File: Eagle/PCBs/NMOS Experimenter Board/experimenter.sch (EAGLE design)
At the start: 45 parts, among them U1 74HC14PW

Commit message: Wow, 92 transistors and 8 LEDs
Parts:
- added D2, D3, D4, D5, D6, D7, D8, D9: (no value), ellajameson-core:LED0603
- added DRAINA100, DRAINA101, DRAINA102, DRAINA103, DRAINA104, DRAINA105, DRAINA106, DRAINA107, DRAINA108, DRAINA109, DRAINA110, DRAINA111, DRAINA112, DRAINA2, DRAINA21, DRAINA22, DRAINA23, DRAINA24, DRAINA25, DRAINA26, DRAINA27, DRAINA28, DRAINA29, DRAINA3, DRAINA30, DRAINA31, DRAINA32, DRAINA33, DRAINA34, DRAINA35, DRAINA36, DRAINA37, DRAINA38, DRAINA39, DRAINA4, DRAINA40, DRAINA41, DRAINA42, DRAINA43, DRAINA44, DRAINA45, DRAINA46, DRAINA47, DRAINA48, DRAINA49, DRAINA5, DRAINA50, DRAINA51, DRAINA52, DRAINA53, DRAINA54, DRAINA55, DRAINA56, DRAINA57, DRAINA58, DRAINA59, DRAINA60, DRAINA61, DRAINA62, DRAINA63, DRAINA64, DRAINA65, DRAINA66, DRAINA67, DRAINA68, DRAINA69, DRAINA70, DRAINA71, DRAINA72, DRAINA73, DRAINA74, DRAINA75, DRAINA76, DRAINA77, DRAINA78, DRAINA79, DRAINA80, DRAINA81, DRAINA82, DRAINA83, DRAINA84, DRAINA85, DRAINA86, DRAINA87, DRAINA88, DRAINA89, DRAINA90, DRAINA91, DRAINA92, DRAINA93, DRAINA94, DRAINA95, DRAINA96, DRAINA97, DRAINA98, DRAINA99, DRAINB100, DRAINB101, DRAINB102, DRAINB103, DRAINB104, DRAINB105, DRAINB106, DRAINB107, DRAINB108, DRAINB109, DRAINB110, DRAINB111, DRAINB112, DRAINB2, DRAINB21, DRAINB22, DRAINB23, DRAINB24, DRAINB25, DRAINB26, DRAINB27, DRAINB28, DRAINB29, DRAINB3, DRAINB30, DRAINB31, DRAINB32, DRAINB33, DRAINB34, DRAINB35, DRAINB36, DRAINB37, DRAINB38, DRAINB39, DRAINB4, DRAINB40, DRAINB41, DRAINB42, DRAINB43, DRAINB44, DRAINB45, DRAINB46, DRAINB47, DRAINB48, DRAINB49, DRAINB5, DRAINB50, DRAINB51, DRAINB52, DRAINB53, DRAINB54, DRAINB55, DRAINB56, DRAINB57, DRAINB58, DRAINB59, DRAINB60, DRAINB61, DRAINB62, DRAINB63, DRAINB64, DRAINB65, DRAINB66, DRAINB67, DRAINB68, DRAINB69, DRAINB70, DRAINB71, DRAINB72, DRAINB73, DRAINB74, DRAINB75, DRAINB76, DRAINB77, DRAINB78, DRAINB79, DRAINB80, DRAINB81, DRAINB82, DRAINB83, DRAINB84, DRAINB85, DRAINB86, DRAINB87, DRAINB88, DRAINB89, DRAINB90, DRAINB91, DRAINB92, DRAINB93, DRAINB94, DRAINB95, DRAINB96, DRAINB97, DRAINB98, DRAINB99, GATEA100, GATEA101, GATEA102, GATEA103, GATEA104, GATEA105, GATEA106, GATEA107, GATEA108, GATEA109, GATEA110, GATEA111, GATEA112, GATEA2, GATEA21, GATEA22, GATEA23, GATEA24, GATEA25, GATEA26, GATEA27, GATEA28, GATEA29, GATEA3, GATEA30, GATEA31, GATEA32, GATEA33, GATEA34, GATEA35, GATEA36, GATEA37, GATEA38, GATEA39, GATEA4, GATEA40, GATEA41, GATEA42, GATEA43, GATEA44, GATEA45, GATEA46, GATEA47, GATEA48, GATEA49, GATEA5, GATEA50, GATEA51, GATEA52, GATEA53, GATEA54, GATEA55, GATEA56, GATEA57, GATEA58, GATEA59, GATEA60, GATEA61, GATEA62, GATEA63, GATEA64, GATEA65, GATEA66, GATEA67, GATEA68, GATEA69, GATEA70, GATEA71, GATEA72, GATEA73, GATEA74, GATEA75, GATEA76, GATEA77, GATEA78, GATEA79, GATEA80, GATEA81, GATEA82, GATEA83, GATEA84, GATEA85, GATEA86, GATEA87, GATEA88, GATEA89, GATEA90, GATEA91, GATEA92, GATEA93, GATEA94, GATEA95, GATEA96, GATEA97, GATEA98, GATEA99, GATEB100, GATEB101, GATEB102, GATEB103, GATEB104, GATEB105, GATEB106, GATEB107, GATEB108, GATEB109, GATEB110, GATEB111, GATEB112, GATEB2, GATEB21, GATEB22, GATEB23, GATEB24, GATEB25, GATEB26, GATEB27, GATEB28, GATEB29, GATEB3, GATEB30, GATEB31, GATEB32, GATEB33, GATEB34, GATEB35, GATEB36, GATEB37, GATEB38, GATEB39, GATEB4, GATEB40, GATEB41, GATEB42, GATEB43, GATEB44, GATEB45, GATEB46, GATEB47, GATEB48, GATEB49, GATEB5, GATEB50, GATEB51, GATEB52, GATEB53, GATEB54, GATEB55, GATEB56, GATEB57, GATEB58, GATEB59, GATEB60, GATEB61, GATEB62, GATEB63, GATEB64, GATEB65, GATEB66, GATEB67, GATEB68, GATEB69, GATEB70, GATEB71, GATEB72, GATEB73, GATEB74, GATEB75, GATEB76, GATEB77, GATEB78, GATEB79, GATEB80, GATEB81, GATEB82, GATEB83, GATEB84, GATEB85, GATEB86, GATEB87, GATEB88, GATEB89, GATEB90, GATEB91, GATEB92, GATEB93, GATEB94, GATEB95, GATEB96, GATEB97, GATEB98, GATEB99, LED2, LED3, LED4, LED5, LED6, LED7, LED8, LED9, SOURCEA100, SOURCEA101, SOURCEA102, SOURCEA103, SOURCEA104, SOURCEA105, SOURCEA106, SOURCEA107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: TPTHT, ellajameson-core:TPTHT
- added JD100, JD101, JD102, JD103, JD104, JD105, JD106, JD107, JD108, JD109, JD110, JD111, JD112, JD2, JD21, JD22, JD23, JD24, JD25, JD26, JD27, JD28, JD29, JD3, JD30, JD31, JD32, JD33, JD34, JD35, JD36, JD37, JD38, JD39, JD4, JD40, JD41, JD42, JD43, JD44, JD45, JD46, JD47, JD48, JD49, JD5, JD50, JD51, JD52, JD53, JD54, JD55, JD56, JD57, JD58, JD59, JD60, JD61, JD62, JD63, JD64, JD65, JD66, JD67, JD68, JD69, JD70, JD71, JD72, JD73, JD74, JD75, JD76, JD77, JD78, JD79, JD80, JD81, JD82, JD83, JD84, JD85, JD86, JD87, JD88, JD89, JD90, JD91, JD92, JD93, JD94, JD95, JD96, JD97, JD98, JD99, JN100, JN101, JN102, JN103, JN104, JN105, JN106, JN107, JN108, JN109, JN110, JN111, JN112, JN2, JN21, JN22, JN23, JN24, JN25, JN26, JN27, JN28, JN29, JN3, JN30, JN31, JN32, JN33, JN34, JN35, JN36, JN37, JN38, JN39, JN4, JN40, JN41, JN42, JN43, JN44, JN45, JN46, JN47, JN48, JN49, JN5, JN50, JN51, JN52, JN53, JN54, JN55, JN56, JN57, JN58, JN59, JN60, JN61, JN62, JN63, JN64, JN65, JN66, JN67, JN68, JN69, JN70, JN71, JN72, JN73, JN74, JN75, JN76, JN77, JN78, JN79, JN80, JN81, JN82, JN83, JN84, JN85, JN86, JN87, JN88, JN89, JN90, JN91, JN92, JN93, JN94, JN95, JN96, JN97, JN98, JN99, JP100, JP101, JP102, JP103, JP104, JP105, JP106, JP107, JP108, JP109, JP110, JP111, JP112, JP2, JP21, JP22, JP23, JP24, JP25, JP26, JP27, JP28, JP29, JP3, JP30, JP31, JP32, JP33, JP34, JP35, JP36, JP37, JP38, JP39, JP4, JP40, JP41, JP42, JP43, JP44, JP45, JP46, JP47, JP48, JP49, JP5, JP50, JP51, JP52, JP53, JP54, JP55, JP56, JP57, JP58, JP59, JP60, JP61, JP62, JP63, JP64, JP65, JP66, JP67, JP68, JP69, JP70, JP71, JP72, JP73, JP74, JP75, JP76, JP77, JP78, JP79, JP80, JP81, JP82, JP83, JP84, JP85, JP86, JP87, JP88, JP89, JP90, JP91, JP92, JP93, JP94, JP95, JP96, JP97, JP98, JP99, JS100, JS101, JS102, JS103, JS104, JS105, JS106, JS107, JS108, JS109, JS110, JS111, JS112, JS2, JS21, JS22, JS23, JS24, JS25, JS26, JS27, JS28, JS29, JS3, JS30, JS31, JS32, JS33, JS34, JS35, JS36, JS37, JS38, JS39, JS4, JS40, JS41, JS42, JS43, JS44, JS45, JS46, JS47, JS48, JS49, JS5, JS50, JS51, JS52, JS53, JS54, JS55, JS56, JS57, JS58, JS59, JS60, JS61, JS62, JS63, JS64, JS65, JS66, JS67, JS68, JS69, JS70, JS71, JS72, JS73, JS74, JS75, JS76, JS77, JS78, JS79, JS80, JS81, JS82, JS83, JS84, JS85, JS86, JS87, JS88, JS89, JS90, JS91, JS92, JS93, JS94, JS95, JS96, JS97, JS98, JS99: SJ_NO_THIN, ellajameson-core:SJ_NO_THIN
- added Q100, Q101, Q102, Q103, Q104, Q105, Q106, Q107, Q108, Q109, Q110, Q111, Q112, Q113, Q114, Q115, Q116, Q117, Q118, Q119, Q120, Q2, Q25, Q26, Q27, Q28, Q29, Q3, Q30, Q31, Q32, Q33, Q34, Q35, Q36, Q37, Q38, Q39, Q4, Q40, Q41, Q42, Q43, Q44, Q45, Q46, Q47, Q48, Q49, Q5, Q50, Q51, Q52, Q53, Q54, Q55, Q56, Q57, Q58, Q59, Q6, Q60, Q61, Q62, Q63, Q64, Q65, Q66, Q67, Q68, Q69, Q7, Q70, Q71, Q72, Q73, Q74, Q75, Q76, Q77, Q78, Q79, Q8, Q80, Q81, Q82, Q83, Q84, Q85, Q86, Q87, Q88, Q89, Q9, Q90, Q91, Q92, Q93, Q94, Q95, Q96, Q97, Q98, Q99: 2N7002, ellajameson-core:2N7002
- added R100, R101, R102, R103, R104, R105, R106, R107, R108, R109, R110, R111, R112, R113, R114, R115, R116, R117, R118, R119, R120, R121, R122, R123, R124, R125, R126, R127, R128, R129, R130, R131, R132, R25, R26, R27, R28, R29, R30, R31, R32, R33, R34, R35, R36, R37, R38, R39, R40, R41, R42, R43, R44, R45, R46, R47, R48, R49, R50, R51, R52, R53, R54, R55, R56, R57, R58, R59, R60, R61, R62, R63, R64, R65, R66, R67, R68, R69, R70, R71, R72, R73, R74, R79, R80, R83, R84, R87, R88, R91, R92, R95, R96, R97, R98, R99: 10k, ellajameson-core:RES0603
- added R2, R3, R4, R5, R6, R7, R8, R9: 330, ellajameson-core:RES0603
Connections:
- new net N$10: D3.A, R3.1
- new net N$100: JP4.2, R27.1
- new net N$101: JN4.2, JS4.2, Q27.S, SOURCEA4.S, SOURCEB4.S
- new net N$102: DRAINA4.S, DRAINB4.S, JD3.1, JD4.2, JP4.1, JS51.1, Q27.D
- new net N$103: GATEA4.S, GATEB4.S, Q27.G
- new net N$104: JP5.2, R28.1
- new net N$105: JN5.2, JS5.2, Q28.S, SOURCEA5.S, SOURCEB5.S
- new net N$106: DRAINA5.S, DRAINB5.S, JD4.1, JD5.2, JP5.1, JS52.1, Q28.D
- new net N$107: GATEA5.S, GATEB5.S, Q28.G
- new net N$108: JP21.2, R29.1
- new net N$109: JN21.2, JS21.2, Q29.S, SOURCEA21.S, SOURCEB21.S
- new net N$11: LED3.S, Q3.G
- new net N$110: DRAINA21.S, DRAINB21.S, JD21.2, JD5.1, JP21.1, JS53.1, Q29.D
- new net N$111: GATEA21.S, GATEB21.S, Q29.G
- new net N$112: JP22.2, R30.1
- new net N$113: JN22.2, JS22.2, Q30.S, SOURCEA22.S, SOURCEB22.S
- new net N$114: DRAINA22.S, DRAINB22.S, JD21.1, JD22.2, JP22.1, JS54.1, Q30.D
- new net N$115: GATEA22.S, GATEB22.S, Q30.G
- new net N$116: JP23.2, R31.1
- new net N$117: JN23.2, JS23.2, Q31.S, SOURCEA23.S, SOURCEB23.S
- new net N$118: DRAINA23.S, DRAINB23.S, JD22.1, JD23.2, JP23.1, JS55.1, Q31.D
- new net N$119: GATEA23.S, GATEB23.S, Q31.G
- new net N$12: D3.K, Q3.D
- new net N$120: JP24.2, R32.1
- new net N$121: JN24.2, JS24.2, Q32.S, SOURCEA24.S, SOURCEB24.S
- new net N$122: DRAINA24.S, DRAINB24.S, JD23.1, JD24.2, JP24.1, JS56.1, Q32.D
- new net N$123: GATEA24.S, GATEB24.S, Q32.G
- new net N$124: JP25.2, R33.1
- new net N$125: JN25.2, JS25.2, Q33.S, SOURCEA25.S, SOURCEB25.S
- new net N$126: DRAINA25.S, DRAINB25.S, JD24.1, JD25.2, JP25.1, JS57.1, Q33.D
- new net N$127: GATEA25.S, GATEB25.S, Q33.G
- new net N$128: JP26.2, R34.1
- new net N$129: JN26.2, JS26.2, Q34.S, SOURCEA26.S, SOURCEB26.S
- new net N$13: D4.A, R4.1
- new net N$130: DRAINA26.S, DRAINB26.S, JD25.1, JD26.2, JP26.1, JS58.1, Q34.D
- new net N$131: GATEA26.S, GATEB26.S, Q34.G
- new net N$132: JP27.2, R35.1
- new net N$133: JN27.2, JS27.2, Q35.S, SOURCEA27.S, SOURCEB27.S
- new net N$134: DRAINA27.S, DRAINB27.S, JD26.1, JD27.2, JP27.1, JS59.1, Q35.D
- new net N$135: GATEA27.S, GATEB27.S, Q35.G
- new net N$136: JP28.2, R36.1
- new net N$137: JN28.2, JS28.2, Q36.S, SOURCEA28.S, SOURCEB28.S
- new net N$138: DRAINA28.S, DRAINB28.S, JD27.1, JD28.2, JP28.1, JS60.1, Q36.D
- new net N$139: GATEA28.S, GATEB28.S, Q36.G
- new net N$14: LED4.S, Q4.G
- new net N$140: JP29.2, R37.1
- new net N$141: JN29.2, JS29.2, Q37.S, SOURCEA29.S, SOURCEB29.S
- new net N$142: DRAINA29.S, DRAINB29.S, JD28.1, JD29.2, JP29.1, JS61.1, Q37.D
- new net N$143: GATEA29.S, GATEB29.S, Q37.G
- new net N$144: JP30.2, R38.1
- new net N$145: JN30.2, JS30.2, Q38.S, SOURCEA30.S, SOURCEB30.S
- new net N$146: DRAINA30.S, DRAINB30.S, JD29.1, JD30.2, JP30.1, JS62.1, Q38.D
- new net N$147: GATEA30.S, GATEB30.S, Q38.G
- new net N$148: JP31.2, R39.1
- new net N$149: JN31.2, JS31.2, Q39.S, SOURCEA31.S, SOURCEB31.S
- new net N$15: D4.K, Q4.D
- new net N$150: DRAINA31.S, DRAINB31.S, JD30.1, JD31.2, JP31.1, JS63.1, Q39.D
- new net N$151: GATEA31.S, GATEB31.S, Q39.G
- new net N$152: JP32.2, R40.1
- new net N$153: JN32.2, JS32.2, Q40.S, SOURCEA32.S, SOURCEB32.S
- new net N$154: DRAINA32.S, DRAINB32.S, JD31.1, JD32.2, JP32.1, JS64.1, Q40.D
- new net N$155: GATEA32.S, GATEB32.S, Q40.G
- new net N$156: JP33.2, R41.1
- new net N$157: JN33.2, JS33.2, Q41.S, SOURCEA33.S, SOURCEB33.S
- new net N$158: DRAINA33.S, DRAINB33.S, JD33.2, JP33.1, JS2.1, Q41.D
- new net N$159: GATEA33.S, GATEB33.S, Q41.G
- new net N$16: D5.A, R5.1
- new net N$160: JP34.2, R42.1
- new net N$161: JN34.2, JS34.2, Q42.S, SOURCEA34.S, SOURCEB34.S
- new net N$162: DRAINA34.S, DRAINB34.S, JD33.1, JD34.2, JP34.1, JS3.1, Q42.D
- new net N$163: GATEA34.S, GATEB34.S, Q42.G
- new net N$164: JP35.2, R43.1
- new net N$165: JN35.2, JS35.2, Q43.S, SOURCEA35.S, SOURCEB35.S
- new net N$166: DRAINA35.S, DRAINB35.S, JD34.1, JD35.2, JP35.1, JS4.1, Q43.D
- new net N$167: GATEA35.S, GATEB35.S, Q43.G
- new net N$168: JP36.2, R44.1
- new net N$169: JN36.2, JS36.2, Q44.S, SOURCEA36.S, SOURCEB36.S
- new net N$17: LED5.S, Q5.G
- new net N$170: DRAINA36.S, DRAINB36.S, JD35.1, JD36.2, JP36.1, JS5.1, Q44.D
- new net N$171: GATEA36.S, GATEB36.S, Q44.G
- new net N$172: JP37.2, R45.1
- new net N$173: JN37.2, JS37.2, Q45.S, SOURCEA37.S, SOURCEB37.S
- new net N$174: DRAINA37.S, DRAINB37.S, JD36.1, JD37.2, JP37.1, JS21.1, Q45.D
- new net N$175: GATEA37.S, GATEB37.S, Q45.G
- new net N$176: JP38.2, R46.1
- new net N$177: JN38.2, JS38.2, Q46.S, SOURCEA38.S, SOURCEB38.S
- new net N$178: DRAINA38.S, DRAINB38.S, JD37.1, JD38.2, JP38.1, JS22.1, Q46.D
- new net N$179: GATEA38.S, GATEB38.S, Q46.G
- new net N$18: D5.K, Q5.D
- new net N$180: JP39.2, R47.1
- new net N$181: JN39.2, JS39.2, Q47.S, SOURCEA39.S, SOURCEB39.S
- new net N$182: DRAINA39.S, DRAINB39.S, JD38.1, JD39.2, JP39.1, JS23.1, Q47.D
- new net N$183: GATEA39.S, GATEB39.S, Q47.G
- new net N$184: JP40.2, R48.1
- new net N$185: JN40.2, JS40.2, Q48.S, SOURCEA40.S, SOURCEB40.S
- new net N$186: DRAINA40.S, DRAINB40.S, JD39.1, JD40.2, JP40.1, JS24.1, Q48.D
- new net N$187: GATEA40.S, GATEB40.S, Q48.G
- new net N$188: JP41.2, R49.1
- new net N$189: JN41.2, JS41.2, Q49.S, SOURCEA41.S, SOURCEB41.S
- new net N$19: D6.A, R6.1
- new net N$190: DRAINA41.S, DRAINB41.S, JD40.1, JD41.2, JP41.1, JS25.1, Q49.D
- new net N$191: GATEA41.S, GATEB41.S, Q49.G
- new net N$192: JP42.2, R50.1
- new net N$193: JN42.2, JS42.2, Q50.S, SOURCEA42.S, SOURCEB42.S
- new net N$194: DRAINA42.S, DRAINB42.S, JD41.1, JD42.2, JP42.1, JS26.1, Q50.D
- new net N$195: GATEA42.S, GATEB42.S, Q50.G
- new net N$196: JP43.2, R51.1
- new net N$197: JN43.2, JS43.2, Q51.S, SOURCEA43.S, SOURCEB43.S
- new net N$198: DRAINA43.S, DRAINB43.S, JD42.1, JD43.2, JP43.1, JS27.1, Q51.D
- new net N$199: GATEA43.S, GATEB43.S, Q51.G
- new net N$20: LED6.S, Q6.G
- new net N$200: JP44.2, R52.1
- new net N$201: JN44.2, JS44.2, Q52.S, SOURCEA44.S, SOURCEB44.S
- new net N$202: DRAINA44.S, DRAINB44.S, JD43.1, JD44.2, JP44.1, JS28.1, Q52.D
- new net N$203: GATEA44.S, GATEB44.S, Q52.G
- new net N$204: JP45.2, R53.1
- new net N$205: JN45.2, JS45.2, Q53.S, SOURCEA45.S, SOURCEB45.S
- new net N$206: DRAINA45.S, DRAINB45.S, JD44.1, JD45.2, JP45.1, JS29.1, Q53.D
- new net N$207: GATEA45.S, GATEB45.S, Q53.G
- new net N$208: JP46.2, R54.1
- new net N$209: JN46.2, JS46.2, Q54.S, SOURCEA46.S, SOURCEB46.S
- new net N$21: D6.K, Q6.D
- new net N$210: DRAINA46.S, DRAINB46.S, JD45.1, JD46.2, JP46.1, JS30.1, Q54.D
- new net N$211: GATEA46.S, GATEB46.S, Q54.G
- new net N$212: JP47.2, R55.1
- new net N$213: JN47.2, JS47.2, Q55.S, SOURCEA47.S, SOURCEB47.S
- new net N$214: DRAINA47.S, DRAINB47.S, JD46.1, JD47.2, JP47.1, JS31.1, Q55.D
- new net N$215: GATEA47.S, GATEB47.S, Q55.G
- new net N$216: JP48.2, R56.1
- new net N$217: JN48.2, JS48.2, Q56.S, SOURCEA48.S, SOURCEB48.S
- new net N$218: DRAINA48.S, DRAINB48.S, JD47.1, JD48.2, JP48.1, JS32.1, Q56.D
- new net N$219: GATEA48.S, GATEB48.S, Q56.G
- new net N$22: D7.A, R7.1
- new net N$220: JP49.2, R57.1
- new net N$221: JN49.2, JS49.2, Q57.S, SOURCEA49.S, SOURCEB49.S
- new net N$222: DRAINA49.S, DRAINB49.S, JD49.2, JP49.1, JS65.1, Q57.D
- new net N$223: GATEA49.S, GATEB49.S, Q57.G
- new net N$224: JP50.2, R58.1
- new net N$225: JN50.2, JS50.2, Q58.S, SOURCEA50.S, SOURCEB50.S
- new net N$226: DRAINA50.S, DRAINB50.S, JD49.1, JD50.2, JP50.1, JS66.1, Q58.D
- new net N$227: GATEA50.S, GATEB50.S, Q58.G
- new net N$228: JP51.2, R59.1
- new net N$229: JN51.2, JS51.2, Q59.S, SOURCEA51.S, SOURCEB51.S
- new net N$23: LED7.S, Q7.G
- new net N$230: DRAINA51.S, DRAINB51.S, JD50.1, JD51.2, JP51.1, JS67.1, Q59.D
- new net N$231: GATEA51.S, GATEB51.S, Q59.G
- new net N$232: JP52.2, R60.1
- new net N$233: JN52.2, JS52.2, Q60.S, SOURCEA52.S, SOURCEB52.S
- new net N$234: DRAINA52.S, DRAINB52.S, JD51.1, JD52.2, JP52.1, JS68.1, Q60.D
- new net N$235: GATEA52.S, GATEB52.S, Q60.G
- new net N$236: JP53.2, R61.1
- new net N$237: JN53.2, JS53.2, Q61.S, SOURCEA53.S, SOURCEB53.S
- new net N$238: DRAINA53.S, DRAINB53.S, JD52.1, JD53.2, JP53.1, JS69.1, Q61.D
- new net N$239: GATEA53.S, GATEB53.S, Q61.G
- new net N$24: D7.K, Q7.D
- new net N$240: JP54.2, R62.1
- new net N$241: JN54.2, JS54.2, Q62.S, SOURCEA54.S, SOURCEB54.S
- new net N$242: DRAINA54.S, DRAINB54.S, JD53.1, JD54.2, JP54.1, JS70.1, Q62.D
- new net N$243: GATEA54.S, GATEB54.S, Q62.G
- new net N$244: JP55.2, R63.1
- new net N$245: JN55.2, JS55.2, Q63.S, SOURCEA55.S, SOURCEB55.S
- new net N$246: DRAINA55.S, DRAINB55.S, JD54.1, JD55.2, JP55.1, JS71.1, Q63.D
- new net N$247: GATEA55.S, GATEB55.S, Q63.G
- new net N$248: JP56.2, R64.1
- new net N$249: JN56.2, JS56.2, Q64.S, SOURCEA56.S, SOURCEB56.S
- new net N$25: D8.A, R8.1
- new net N$250: DRAINA56.S, DRAINB56.S, JD55.1, JD56.2, JP56.1, JS72.1, Q64.D
- new net N$251: GATEA56.S, GATEB56.S, Q64.G
- new net N$252: JP57.2, R65.1
- new net N$253: JN57.2, JS57.2, Q65.S, SOURCEA57.S, SOURCEB57.S
- new net N$254: DRAINA57.S, DRAINB57.S, JD56.1, JD57.2, JP57.1, JS73.1, Q65.D
- new net N$255: GATEA57.S, GATEB57.S, Q65.G
- new net N$256: JP58.2, R66.1
- new net N$257: JN58.2, JS58.2, Q66.S, SOURCEA58.S, SOURCEB58.S
- new net N$258: DRAINA58.S, DRAINB58.S, JD57.1, JD58.2, JP58.1, JS74.1, Q66.D
- new net N$259: GATEA58.S, GATEB58.S, Q66.G
- new net N$26: LED8.S, Q8.G
- new net N$260: JP59.2, R67.1
- new net N$261: JN59.2, JS59.2, Q67.S, SOURCEA59.S, SOURCEB59.S
- new net N$262: DRAINA59.S, DRAINB59.S, JD58.1, JD59.2, JP59.1, JS75.1, Q67.D
- new net N$263: GATEA59.S, GATEB59.S, Q67.G
- new net N$264: JP60.2, R68.1
- new net N$265: JN60.2, JS60.2, Q68.S, SOURCEA60.S, SOURCEB60.S
- new net N$266: DRAINA60.S, DRAINB60.S, JD59.1, JD60.2, JP60.1, JS76.1, Q68.D
- new net N$267: GATEA60.S, GATEB60.S, Q68.G
- new net N$268: JP61.2, R69.1
- new net N$269: JN61.2, JS61.2, Q69.S, SOURCEA61.S, SOURCEB61.S
- new net N$27: D8.K, Q8.D
- new net N$270: DRAINA61.S, DRAINB61.S, JD60.1, JD61.2, JP61.1, JS77.1, Q69.D
- new net N$271: GATEA61.S, GATEB61.S, Q69.G
- new net N$272: JP62.2, R70.1
- new net N$273: JN62.2, JS62.2, Q70.S, SOURCEA62.S, SOURCEB62.S
- new net N$274: DRAINA62.S, DRAINB62.S, JD61.1, JD62.2, JP62.1, JS78.1, Q70.D
- new net N$275: GATEA62.S, GATEB62.S, Q70.G
- new net N$276: JP63.2, R71.1
- new net N$277: JN63.2, JS63.2, Q71.S, SOURCEA63.S, SOURCEB63.S
- new net N$278: DRAINA63.S, DRAINB63.S, JD62.1, JD63.2, JP63.1, JS79.1, Q71.D
- new net N$279: GATEA63.S, GATEB63.S, Q71.G
- new net N$28: D9.A, R9.1
- new net N$280: JP64.2, R72.1
- new net N$281: JN64.2, JS64.2, Q72.S, SOURCEA64.S, SOURCEB64.S
- new net N$282: DRAINA64.S, DRAINB64.S, JD63.1, JD64.2, JP64.1, JS80.1, Q72.D
- new net N$283: GATEA64.S, GATEB64.S, Q72.G
- new net N$284: JP65.2, R73.1
- new net N$285: JN65.2, JS65.2, Q73.S, SOURCEA65.S, SOURCEB65.S
- new net N$286: DRAINA65.S, DRAINB65.S, JD65.2, JP65.1, JS81.1, Q73.D
- new net N$287: GATEA65.S, GATEB65.S, Q73.G
- new net N$288: JP66.2, R74.1
- new net N$289: JN66.2, JS66.2, Q74.S, SOURCEA66.S, SOURCEB66.S
- new net N$29: LED9.S, Q9.G
- new net N$290: DRAINA66.S, DRAINB66.S, JD65.1, JD66.2, JP66.1, JS82.1, Q74.D
- new net N$291: GATEA66.S, GATEB66.S, Q74.G
- new net N$292: JP67.2, R79.1
- new net N$293: JN67.2, JS67.2, Q75.S, SOURCEA67.S, SOURCEB67.S
- new net N$297: DRAINA67.S, DRAINB67.S, JD66.1, JD67.2, JP67.1, JS83.1, Q75.D
- new net N$30: D9.K, Q9.D
- new net N$301: GATEA67.S, GATEB67.S, Q75.G
- new net N$303: JP68.2, R80.1
- new net N$304: JN68.2, JS68.2, Q76.S, SOURCEA68.S, SOURCEB68.S
- new net N$305: DRAINA68.S, DRAINB68.S, JD67.1, JD68.2, JP68.1, JS84.1, Q76.D
- new net N$307: GATEA68.S, GATEB68.S, Q76.G
- new net N$308: JP69.2, R83.1
- new net N$309: JN69.2, JS69.2, Q77.S, SOURCEA69.S, SOURCEB69.S
- new net N$311: DRAINA69.S, DRAINB69.S, JD68.1, JD69.2, JP69.1, JS85.1, Q77.D
- new net N$312: GATEA69.S, GATEB69.S, Q77.G
- new net N$313: JP70.2, R84.1
- new net N$314: JN70.2, JS70.2, Q78.S, SOURCEA70.S, SOURCEB70.S
- new net N$315: DRAINA70.S, DRAINB70.S, JD69.1, JD70.2, JP70.1, JS86.1, Q78.D
- new net N$316: GATEA70.S, GATEB70.S, Q78.G
- new net N$317: JP71.2, R87.1
- new net N$318: JN71.2, JS71.2, Q79.S, SOURCEA71.S, SOURCEB71.S
- new net N$319: DRAINA71.S, DRAINB71.S, JD70.1, JD71.2, JP71.1, JS87.1, Q79.D
- new net N$320: GATEA71.S, GATEB71.S, Q79.G
- new net N$323: JP72.2, R88.1
- new net N$324: JN72.2, JS72.2, Q80.S, SOURCEA72.S, SOURCEB72.S
- new net N$325: DRAINA72.S, DRAINB72.S, JD71.1, JD72.2, JP72.1, JS88.1, Q80.D
- new net N$326: GATEA72.S, GATEB72.S, Q80.G
- new net N$327: JP73.2, R91.1
- new net N$328: JN73.2, JS73.2, Q81.S, SOURCEA73.S, SOURCEB73.S
- new net N$329: DRAINA73.S, DRAINB73.S, JD72.1, JD73.2, JP73.1, JS89.1, Q81.D
- new net N$330: GATEA73.S, GATEB73.S, Q81.G
- new net N$331: JP74.2, R92.1
- new net N$332: JN74.2, JS74.2, Q82.S, SOURCEA74.S, SOURCEB74.S
- new net N$333: DRAINA74.S, DRAINB74.S, JD73.1, JD74.2, JP74.1, JS90.1, Q82.D
- new net N$334: GATEA74.S, GATEB74.S, Q82.G
- new net N$335: JP75.2, R95.1
- new net N$336: JN75.2, JS75.2, Q83.S, SOURCEA75.S, SOURCEB75.S
- new net N$337: DRAINA75.S, DRAINB75.S, JD74.1, JD75.2, JP75.1, JS91.1, Q83.D
- new net N$338: GATEA75.S, GATEB75.S, Q83.G
- new net N$339: JP76.2, R96.1
- new net N$340: JN76.2, JS76.2, Q84.S, SOURCEA76.S, SOURCEB76.S
- new net N$341: DRAINA76.S, DRAINB76.S, JD75.1, JD76.2, JP76.1, JS92.1, Q84.D
- new net N$342: GATEA76.S, GATEB76.S, Q84.G
- new net N$343: JP77.2, R97.1
- new net N$344: JN77.2, JS77.2, Q85.S, SOURCEA77.S, SOURCEB77.S
- new net N$345: DRAINA77.S, DRAINB77.S, JD76.1, JD77.2, JP77.1, JS93.1, Q85.D
- new net N$346: GATEA77.S, GATEB77.S, Q85.G
- new net N$347: JP78.2, R98.1
- new net N$348: JN78.2, JS78.2, Q86.S, SOURCEA78.S, SOURCEB78.S
- new net N$349: DRAINA78.S, DRAINB78.S, JD77.1, JD78.2, JP78.1, JS94.1, Q86.D
- new net N$350: GATEA78.S, GATEB78.S, Q86.G
- new net N$351: JP79.2, R99.1
- new net N$352: JN79.2, JS79.2, Q87.S, SOURCEA79.S, SOURCEB79.S
- new net N$353: DRAINA79.S, DRAINB79.S, JD78.1, JD79.2, JP79.1, JS95.1, Q87.D
- new net N$354: GATEA79.S, GATEB79.S, Q87.G
- new net N$355: JP80.2, R100.1
- new net N$356: JN80.2, JS80.2, Q88.S, SOURCEA80.S, SOURCEB80.S
- new net N$357: DRAINA80.S, DRAINB80.S, JD79.1, JD80.2, JP80.1, JS96.1, Q88.D
- new net N$358: GATEA80.S, GATEB80.S, Q88.G
- new net N$359: JP81.2, R101.1
- new net N$360: JN81.2, JS81.2, Q89.S, SOURCEA81.S, SOURCEB81.S
- new net N$361: DRAINA81.S, DRAINB81.S, JD81.2, JP81.1, JS97.1, Q89.D
- new net N$362: GATEA81.S, GATEB81.S, Q89.G
- new net N$363: JP82.2, R102.1
- new net N$364: JN82.2, JS82.2, Q90.S, SOURCEA82.S, SOURCEB82.S
- new net N$365: DRAINA82.S, DRAINB82.S, JD81.1, JD82.2, JP82.1, JS98.1, Q90.D
- new net N$366: GATEA82.S, GATEB82.S, Q90.G
- new net N$367: JP83.2, R103.1
- new net N$368: JN83.2, JS83.2, Q91.S, SOURCEA83.S, SOURCEB83.S
- new net N$369: DRAINA83.S, DRAINB83.S, JD82.1, JD83.2, JP83.1, JS99.1, Q91.D
- new net N$370: GATEA83.S, GATEB83.S, Q91.G
- new net N$371: JP84.2, R104.1
- new net N$372: JN84.2, JS84.2, Q92.S, SOURCEA84.S, SOURCEB84.S
- new net N$373: DRAINA84.S, DRAINB84.S, JD83.1, JD84.2, JP84.1, JS100.1, Q92.D
- new net N$374: GATEA84.S, GATEB84.S, Q92.G
- new net N$375: JP85.2, R105.1
- new net N$376: JN85.2, JS85.2, Q93.S, SOURCEA85.S, SOURCEB85.S
- new net N$377: DRAINA85.S, DRAINB85.S, JD84.1, JD85.2, JP85.1, JS101.1, Q93.D
- new net N$378: GATEA85.S, GATEB85.S, Q93.G
- new net N$379: JP86.2, R106.1
- new net N$380: JN86.2, JS86.2, Q94.S, SOURCEA86.S, SOURCEB86.S
- new net N$381: DRAINA86.S, DRAINB86.S, JD85.1, JD86.2, JP86.1, JS102.1, Q94.D
- new net N$382: GATEA86.S, GATEB86.S, Q94.G
- new net N$383: JP87.2, R107.1
- new net N$384: JN87.2, JS87.2, Q95.S, SOURCEA87.S, SOURCEB87.S
- new net N$385: DRAINA87.S, DRAINB87.S, JD86.1, JD87.2, JP87.1, JS103.1, Q95.D
- new net N$386: GATEA87.S, GATEB87.S, Q95.G
- new net N$387: JP88.2, R108.1
- new net N$388: JN88.2, JS88.2, Q96.S, SOURCEA88.S, SOURCEB88.S
- new net N$389: DRAINA88.S, DRAINB88.S, JD87.1, JD88.2, JP88.1, JS104.1, Q96.D
- new net N$390: GATEA88.S, GATEB88.S, Q96.G
- new net N$391: JP89.2, R109.1
- new net N$392: JN89.2, JS89.2, Q97.S, SOURCEA89.S, SOURCEB89.S
- new net N$393: DRAINA89.S, DRAINB89.S, JD88.1, JD89.2, JP89.1, JS105.1, Q97.D
- new net N$394: GATEA89.S, GATEB89.S, Q97.G
- new net N$395: JP90.2, R110.1
- new net N$396: JN90.2, JS90.2, Q98.S, SOURCEA90.S, SOURCEB90.S
- new net N$397: DRAINA90.S, DRAINB90.S, JD89.1, JD90.2, JP90.1, JS106.1, Q98.D
- new net N$398: GATEA90.S, GATEB90.S, Q98.G
- new net N$399: JP91.2, R111.1
- new net N$4: D2.A, R2.1
- new net N$400: JN91.2, JS91.2, Q99.S, SOURCEA91.S, SOURCEB91.S
- new net N$401: DRAINA91.S, DRAINB91.S, JD90.1, JD91.2, JP91.1, JS107.1, Q99.D
- new net N$402: GATEA91.S, GATEB91.S, Q99.G
- new net N$403: JP92.2, R112.1
- new net N$404: JN92.2, JS92.2, Q100.S, SOURCEA92.S, SOURCEB92.S
- new net N$405: DRAINA92.S, DRAINB92.S, JD91.1, JD92.2, JP92.1, JS108.1, Q100.D
- new net N$406: GATEA92.S, GATEB92.S, Q100.G
- new net N$407: JP93.2, R113.1
- new net N$408: JN93.2, JS93.2, Q101.S, SOURCEA93.S, SOURCEB93.S
- new net N$409: DRAINA93.S, DRAINB93.S, JD92.1, JD93.2, JP93.1, JS109.1, Q101.D
- new net N$410: GATEA93.S, GATEB93.S, Q101.G
- new net N$411: JP94.2, R114.1
- new net N$412: JN94.2, JS94.2, Q102.S, SOURCEA94.S, SOURCEB94.S
- new net N$413: DRAINA94.S, DRAINB94.S, JD93.1, JD94.2, JP94.1, JS110.1, Q102.D
- new net N$414: GATEA94.S, GATEB94.S, Q102.G
- new net N$415: JP95.2, R115.1
- new net N$416: JN95.2, JS95.2, Q103.S, SOURCEA95.S, SOURCEB95.S
- new net N$417: DRAINA95.S, DRAINB95.S, JD94.1, JD95.2, JP95.1, JS111.1, Q103.D
- new net N$418: GATEA95.S, GATEB95.S, Q103.G
- new net N$419: JP96.2, R116.1
- new net N$420: JN96.2, JS96.2, Q104.S, SOURCEA96.S, SOURCEB96.S
- new net N$421: DRAINA96.S, DRAINB96.S, JD95.1, JD96.2, JP96.1, JS112.1, Q104.D
- new net N$422: GATEA96.S, GATEB96.S, Q104.G
- new net N$423: JP97.2, R117.1
- new net N$424: JN97.2, JS97.2, Q105.S, SOURCEA97.S, SOURCEB97.S
- new net N$425: DRAINA97.S, DRAINB97.S, JD97.2, JP97.1, Q105.D
- new net N$426: GATEA97.S, GATEB97.S, Q105.G
- new net N$427: JP98.2, R118.1
- new net N$428: JN98.2, JS98.2, Q106.S, SOURCEA98.S, SOURCEB98.S
- new net N$429: DRAINA98.S, DRAINB98.S, JD97.1, JD98.2, JP98.1, Q106.D
- new net N$430: GATEA98.S, GATEB98.S, Q106.G
- new net N$431: JP99.2, R119.1
- new net N$432: JN99.2, JS99.2, Q107.S, SOURCEA99.S, SOURCEB99.S
- new net N$433: DRAINA99.S, DRAINB99.S, JD98.1, JD99.2, JP99.1, Q107.D
- new net N$434: GATEA99.S, GATEB99.S, Q107.G
- new net N$435: JP100.2, R120.1
- new net N$436: JN100.2, JS100.2, Q108.S, SOURCEA100.S, SOURCEB100.S
- new net N$437: DRAINA100.S, DRAINB100.S, JD100.2, JD99.1, JP100.1, Q108.D
- new net N$438: GATEA100.S, GATEB100.S, Q108.G
- new net N$439: JP101.2, R121.1
- new net N$440: JN101.2, JS101.2, Q109.S, SOURCEA101.S, SOURCEB101.S
- new net N$441: DRAINA101.S, DRAINB101.S, JD100.1, JD101.2, JP101.1, Q109.D
- new net N$442: GATEA101.S, GATEB101.S, Q109.G
- new net N$443: JP102.2, R122.1
- new net N$444: JN102.2, JS102.2, Q110.S, SOURCEA102.S, SOURCEB102.S
- new net N$445: DRAINA102.S, DRAINB102.S, JD101.1, JD102.2, JP102.1, Q110.D
- new net N$446: GATEA102.S, GATEB102.S, Q110.G
- new net N$447: JP103.2, R123.1
- new net N$448: JN103.2, JS103.2, Q111.S, SOURCEA103.S, SOURCEB103.S
- new net N$449: DRAINA103.S, DRAINB103.S, JD102.1, JD103.2, JP103.1, Q111.D
- new net N$450: GATEA103.S, GATEB103.S, Q111.G
- new net N$451: JP104.2, R124.1
- new net N$452: JN104.2, JS104.2, Q112.S, SOURCEA104.S, SOURCEB104.S
- new net N$453: DRAINA104.S, DRAINB104.S, JD103.1, JD104.2, JP104.1, Q112.D
- new net N$454: GATEA104.S, GATEB104.S, Q112.G
- new net N$455: JP105.2, R125.1
- new net N$456: JN105.2, JS105.2, Q113.S, SOURCEA105.S, SOURCEB105.S
- new net N$457: DRAINA105.S, DRAINB105.S, JD104.1, JD105.2, JP105.1, Q113.D
- new net N$458: GATEA105.S, GATEB105.S, Q113.G
- new net N$459: JP106.2, R126.1
- new net N$460: JN106.2, JS106.2, Q114.S, SOURCEA106.S, SOURCEB106.S
- new net N$461: DRAINA106.S, DRAINB106.S, JD105.1, JD106.2, JP106.1, Q114.D
- new net N$462: GATEA106.S, GATEB106.S, Q114.G
- new net N$463: JP107.2, R127.1
- new net N$464: JN107.2, JS107.2, Q115.S, SOURCEA107.S, SOURCEB107.S
- new net N$465: DRAINA107.S, DRAINB107.S, JD106.1, JD107.2, JP107.1, Q115.D
- new net N$466: GATEA107.S, GATEB107.S, Q115.G
- new net N$467: JP108.2, R128.1
- new net N$468: JN108.2, JS108.2, Q116.S, SOURCEA108.S, SOURCEB108.S
- new net N$469: DRAINA108.S, DRAINB108.S, JD107.1, JD108.2, JP108.1, Q116.D
- new net N$470: GATEA108.S, GATEB108.S, Q116.G
- new net N$471: JP109.2, R129.1
- new net N$472: JN109.2, JS109.2, Q117.S, SOURCEA109.S, SOURCEB109.S
- new net N$473: DRAINA109.S, DRAINB109.S, JD108.1, JD109.2, JP109.1, Q117.D
- new net N$474: GATEA109.S, GATEB109.S, Q117.G
- new net N$475: JP110.2, R130.1
- new net N$476: JN110.2, JS110.2, Q118.S, SOURCEA110.S, SOURCEB110.S
- new net N$477: DRAINA110.S, DRAINB110.S, JD109.1, JD110.2, JP110.1, Q118.D
- new net N$478: GATEA110.S, GATEB110.S, Q118.G
- new net N$479: JP111.2, R131.1
- new net N$480: JN111.2, JS111.2, Q119.S, SOURCEA111.S, SOURCEB111.S
- new net N$481: DRAINA111.S, DRAINB111.S, JD110.1, JD111.2, JP111.1, Q119.D
- new net N$482: GATEA111.S, GATEB111.S, Q119.G
- new net N$483: JP112.2, R132.1
- new net N$484: JN112.2, JS112.2, Q120.S, SOURCEA112.S, SOURCEB112.S
- new net N$485: DRAINA112.S, DRAINB112.S, JD111.1, JD112.2, JP112.1, Q120.D
- new net N$486: GATEA112.S, GATEB112.S, Q120.G
- new net N$7: LED2.S, Q2.G
- new net N$9: D2.K, Q2.D
- new net N$92: JP2.2, R25.1
- new net N$93: JN2.2, JS2.2, Q25.S, SOURCEA2.S, SOURCEB2.S
- new net N$94: DRAINA2.S, DRAINB2.S, JD2.2, JP2.1, JS49.1, Q25.D
- new net N$95: GATEA2.S, GATEB2.S, Q25.G
- new net N$96: JP3.2, R26.1
- new net N$97: JN3.2, JS3.2, Q26.S, SOURCEA3.S, SOURCEB3.S
- new net N$98: DRAINA3.S, DRAINB3.S, JD2.1, JD3.2, JP3.1, JS50.1, Q26.D
- new net N$99: GATEA3.S, GATEB3.S, Q26.G
- net GND: now also JN100.1, JN101.1, JN102.1, JN103.1, JN104.1, JN105.1, JN106.1, JN107.1, JN108.1, JN109.1, JN110.1, JN111.1, JN112.1, JN2.1, JN21.1, JN22.1, JN23.1, JN24.1, JN25.1, JN26.1, JN27.1, JN28.1, JN29.1, JN3.1, JN30.1, JN31.1, JN32.1, JN33.1, JN34.1, JN35.1, JN36.1, JN37.1, JN38.1, JN39.1, JN4.1, JN40.1, JN41.1, JN42.1, JN43.1, JN44.1, JN45.1, JN46.1, JN47.1, JN48.1, JN49.1, JN5.1, JN50.1, JN51.1, JN52.1, JN53.1, JN54.1, JN55.1, JN56.1, JN57.1, JN58.1, JN59.1, JN60.1, JN61.1, JN62.1, JN63.1, JN64.1, JN65.1, JN66.1, JN67.1, JN68.1, JN69.1, JN70.1, JN71.1, JN72.1, JN73.1, JN74.1, JN75.1, JN76.1, JN77.1, JN78.1, JN79.1, JN80.1, JN81.1, JN82.1, JN83.1, JN84.1, JN85.1, JN86.1, JN87.1, JN88.1, JN89.1, JN90.1, JN91.1, JN92.1, JN93.1, JN94.1, JN95.1, JN96.1, JN97.1, JN98.1, JN99.1, Q2.S, Q3.S, Q4.S, Q5.S, Q6.S, Q7.S, Q8.S, Q9.S
- net VCC: now also R100.2, R101.2, R102.2, R103.2, R104.2, R105.2, R106.2, R107.2, R108.2, R109.2, R110.2, R111.2, R112.2, R113.2, R114.2, R115.2, R116.2, R117.2, R118.2, R119.2, R120.2, R121.2, R122.2, R123.2, R124.2, R125.2, R126.2, R127.2, R128.2, R129.2, R130.2, R131.2, R132.2, R2.2, R25.2, R26.2, R27.2, R28.2, R29.2, R3.2, R30.2, R31.2, R32.2, R33.2, R34.2, R35.2, R36.2, R37.2, R38.2, R39.2, R4.2, R40.2, R41.2, R42.2, R43.2, R44.2, R45.2, R46.2, R47.2, R48.2, R49.2, R5.2, R50.2, R51.2, R52.2, R53.2, R54.2, R55.2, R56.2, R57.2, R58.2, R59.2, R6.2, R60.2, R61.2, R62.2, R63.2, R64.2, R65.2, R66.2, R67.2, R68.2, R69.2, R7.2, R70.2, R71.2, R72.2, R73.2, R74.2, R79.2, R8.2, R80.2, R83.2, R84.2, R87.2, R88.2, R9.2, R91.2, R92.2, R95.2, R96.2, R97.2, R98.2, R99.2
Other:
- note added: "LED Output"
- note added: "NMOS Logic Transistor Cell"
- moved on the sheet: B1, B2, B3, B4, B5, B6, C1, C11, C2, C3, C4, C5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

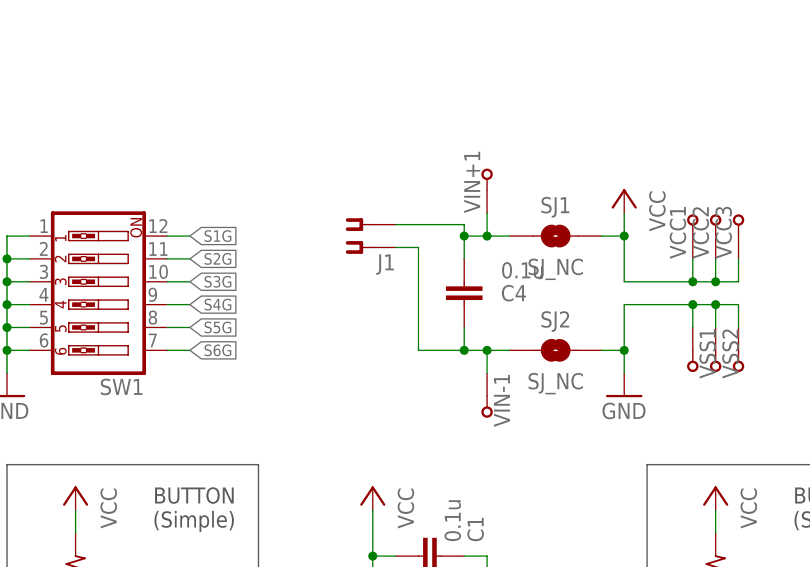
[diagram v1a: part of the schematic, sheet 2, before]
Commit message: Fixed power input connector
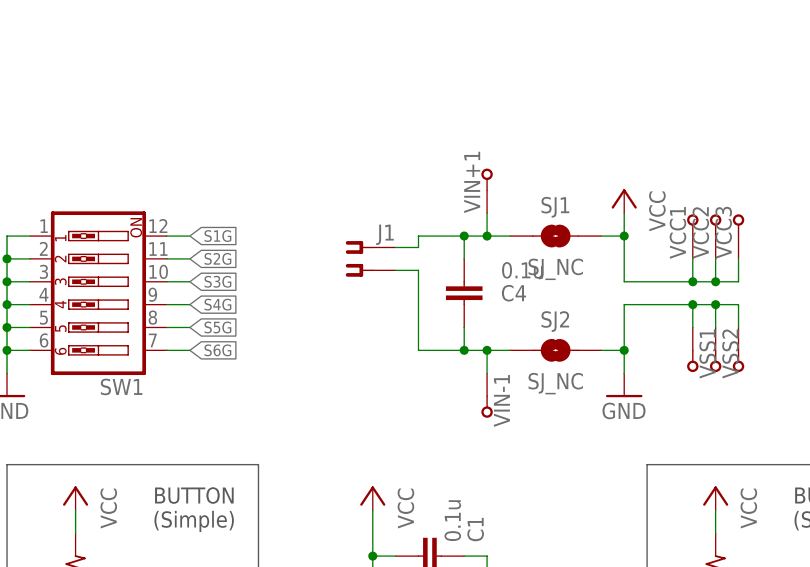
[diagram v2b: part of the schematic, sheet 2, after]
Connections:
- net N$321: now also J1.S1; no longer J1.S
- net N$322: now also J1.S; no longer J1.S1
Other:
- moved on the sheet: J1
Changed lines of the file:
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@@
 <attribute name="VALUE" x="183.261" y="191.516" size="1.778" layer="96" rot="R90"/>
 </instance>
-<instance part="J1" gate="G$1" x="43.18" y="160.02" smashed="yes" rot="R180">
-<attribute name="NAME" x="43.18" y="156.21" size="1.778" layer="95" align="bottom-right"/>
-<attribute name="VALUE" x="43.18" y="163.83" size="1.778" layer="96" rot="R180"/>
+<instance part="J1" gate="G$1" x="43.18" y="157.48" smashed="yes" rot="MR0">
+<attribute name="NAME" x="43.18" y="161.29" size="1.778" layer="95" rot="MR180" align="bottom-right"/>
+<attribute name="VALUE" x="43.18" y="153.67" size="1.778" layer="96" rot="MR0"/>
 </instance>
 <instance part="P+76" gate="VCC" x="68.58" y="165.1" smashed="yes">
@@
 <net name="N$321" class="0">
 <segment>
-<pinref part="J1" gate="G$1" pin="S"/>
-<wire x1="43.18" y1="158.75" x2="45.72" y2="158.75" width="0.1524" layer="91"/>
-<wire x1="45.72" y1="158.75" x2="45.72" y2="147.32" width="0.1524" layer="91"/>
 <wire x1="45.72" y1="147.32" x2="50.8" y2="147.32" width="0.1524" layer="91"/>
 <pinref part="C4" gate="G$1" pin="1"/>
@@
 <junction x="53.34" y="147.32"/>
 <pinref part="SJ2" gate="1" pin="1"/>
+<pinref part="J1" gate="G$1" pin="S1"/>
+<wire x1="43.18" y1="156.21" x2="45.72" y2="156.21" width="0.1524" layer="91"/>
+<wire x1="45.72" y1="156.21" x2="45.72" y2="147.32" width="0.1524" layer="91"/>
 </segment>
 </net>
@@
 <wire x1="53.34" y1="162.56" x2="53.34" y2="160.02" width="0.1524" layer="91"/>
 <wire x1="53.34" y1="160.02" x2="55.88" y2="160.02" width="0.1524" layer="91"/>
-<pinref part="J1" gate="G$1" pin="S1"/>
 <pinref part="C4" gate="G$1" pin="2"/>
-<wire x1="43.18" y1="161.29" x2="50.8" y2="161.29" width="0.1524" layer="91"/>
-<wire x1="50.8" y1="161.29" x2="50.8" y2="160.02" width="0.1524" layer="91"/>
 <wire x1="50.8" y1="160.02" x2="50.8" y2="157.48" width="0.1524" layer="91"/>
 <wire x1="53.34" y1="160.02" x2="50.8" y2="160.02" width="0.1524" layer="91"/>
 <junction x="53.34" y="160.02"/>
+<pinref part="SJ1" gate="1" pin="1"/>
+<pinref part="J1" gate="G$1" pin="S"/>
+<wire x1="43.18" y1="158.75" x2="45.72" y2="158.75" width="0.1524" layer="91"/>
+<wire x1="45.72" y1="158.75" x2="45.72" y2="160.02" width="0.1524" layer="91"/>
+<wire x1="45.72" y1="160.02" x2="50.8" y2="160.02" width="0.1524" layer="91"/>
 <junction x="50.8" y="160.02"/>
-<pinref part="SJ1" gate="1" pin="1"/>
-</segment>
-</net>
+</segment>
+</net>

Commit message: Simplifiied experiment board
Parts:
- removed B1, B2, B3, B4, B5, B6, VCC2, VCC3, VSS2, VSS3: TPTHT, ellajameson-core:TPTHT
- removed C1, C11, C2, C3, C5, C7, C9: 0.1u, ellajameson-core:CAP0603
- removed R75, R76, R77, R78, R81, R82, R85, R86, R89, R90, R93, R94: 10k, ellajameson-core:RES0603
- removed S11, S2, S3, S5, S7, S9: (no value), ellajameson-core:SWITCH-NO-MOMPTS815SJM250SMTRLFS
- removed SW1: (no value), ellajameson-core:SW_DIP-6
- removed U1: 74HC14PW, ellajameson-core:74HC14PW
- added D10, D11, D12, D13, D14, D15, D16, D17, D18, D19, D20, D21, D22, D23, D24: (no value), ellajameson-core:LED0603
- added LED10, LED11, LED12, LED13, LED14, LED15, LED16, LED17, LED18, LED19, LED20, LED21, LED22, LED23, LED24: TPTHT, ellajameson-core:TPTHT
- added Q10, Q11, Q12, Q13, Q14, Q15, Q16, Q17, Q18, Q19, Q20, Q21, Q22, Q23, Q24: 2N7002, ellajameson-core:2N7002
- added R10, R11, R12, R13, R14, R15, R16, R17, R18, R19, R20, R21, R22, R23, R24: 330, ellajameson-core:RES0603
- SJ1, SJ2: value SJ_NC -> SJ_NO_THIN; device ellajameson-core:SJ_NC -> ellajameson-core:SJ_NO_THIN
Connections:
- removed net N$294: C3.1, R78.1, U1E.I
- removed net N$295: B4.S, U1C.O
- removed net N$296: B3.S, U1D.O
- removed net N$298: C5.1, R82.1, U1D.I
- removed net N$299: B2.S, U1E.O
- removed net N$300: B1.S, U1F.O
- removed net N$302: C7.1, R86.1, U1C.I
- removed net N$306: C9.1, R90.1, U1B.I
- removed net N$310: C11.1, R94.1, U1A.I
- removed net N$5: B6.S, U1A.O
- removed net N$8: C2.1, R76.1, U1F.I
- removed net S1G: R75.1, R76.2, S2.S, SW1.12
- removed net S2G: R77.1, R78.2, S3.S, SW1.11
- removed net S3G: R81.1, R82.2, S5.S, SW1.10
- removed net S4G: R85.1, R86.2, S7.S, SW1.9
- removed net S5G: R89.1, R90.2, S9.S, SW1.8
- removed net S6G: R93.1, R94.2, S11.S, SW1.7
- new net N$2: D10.A, R10.1
- new net N$3: LED10.S, Q10.G
- new net N$31: D11.A, R11.1
- new net N$32: LED11.S, Q11.G
- new net N$33: D11.K, Q11.D
- new net N$34: D12.A, R12.1
- new net N$35: LED12.S, Q12.G
- new net N$36: D12.K, Q12.D
- new net N$37: D13.A, R13.1
- new net N$38: LED13.S, Q13.G
- new net N$39: D13.K, Q13.D
- new net N$40: D14.A, R14.1
- new net N$41: LED14.S, Q14.G
- new net N$42: D14.K, Q14.D
- new net N$43: D15.A, R15.1
- new net N$44: LED15.S, Q15.G
- new net N$45: D15.K, Q15.D
- new net N$46: D16.A, R16.1
- new net N$47: LED16.S, Q16.G
- new net N$48: D16.K, Q16.D
- new net N$49: D17.A, R17.1
- new net N$50: LED17.S, Q17.G
- new net N$51: D17.K, Q17.D
- new net N$52: D18.A, R18.1
- new net N$53: LED18.S, Q18.G
- new net N$54: D18.K, Q18.D
- new net N$55: D19.A, R19.1
- new net N$56: LED19.S, Q19.G
- new net N$57: D19.K, Q19.D
- new net N$58: D20.A, R20.1
- new net N$59: LED20.S, Q20.G
- new net N$60: D20.K, Q20.D
- new net N$61: D21.A, R21.1
- new net N$62: LED21.S, Q21.G
- new net N$63: D21.K, Q21.D
- new net N$64: D22.A, R22.1
- new net N$65: LED22.S, Q22.G
- new net N$66: D22.K, Q22.D
- new net N$67: D23.A, R23.1
- new net N$68: LED23.S, Q23.G
- new net N$69: D23.K, Q23.D
- new net N$70: D24.A, R24.1
- new net N$71: LED24.S, Q24.G
- new net N$72: D24.K, Q24.D
- net GND: now also Q10.S, Q11.S, Q12.S, Q13.S, Q14.S, Q15.S, Q16.S, Q17.S, Q18.S, Q19.S, Q20.S, Q21.S, Q22.S, Q23.S, Q24.S; no longer C1.2, C11.2, C2.2, C3.2, C5.2, C7.2, C9.2, S11.P, S2.P, S3.P, S5.P, S7.P, S9.P, SW1.1, SW1.2, SW1.3, SW1.4, SW1.5, SW1.6, U1G$1.V-, VSS2.S, VSS3.S
- net N$6: now also D10.K, Q10.D; no longer B5.S, U1B.O
- net VCC: now also R10.2, R11.2, R12.2, R13.2, R14.2, R15.2, R16.2, R17.2, R18.2, R19.2, R20.2, R21.2, R22.2, R23.2, R24.2; no longer C1.1, R75.2, R77.2, R81.2, R85.2, R89.2, R93.2, U1G$1.V+, VCC2.S, VCC3.S
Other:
- note removed: "BUTTON (Simple)"
